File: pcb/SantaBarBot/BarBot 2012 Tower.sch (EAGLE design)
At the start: 52 parts, among them J2 POWER_JACKSLT, U1 ATMEGA328P, U2 SN75HVD179D, U3 742G04DBVR, U4 LMV324IDR, U5 L298, Y1 16MHz

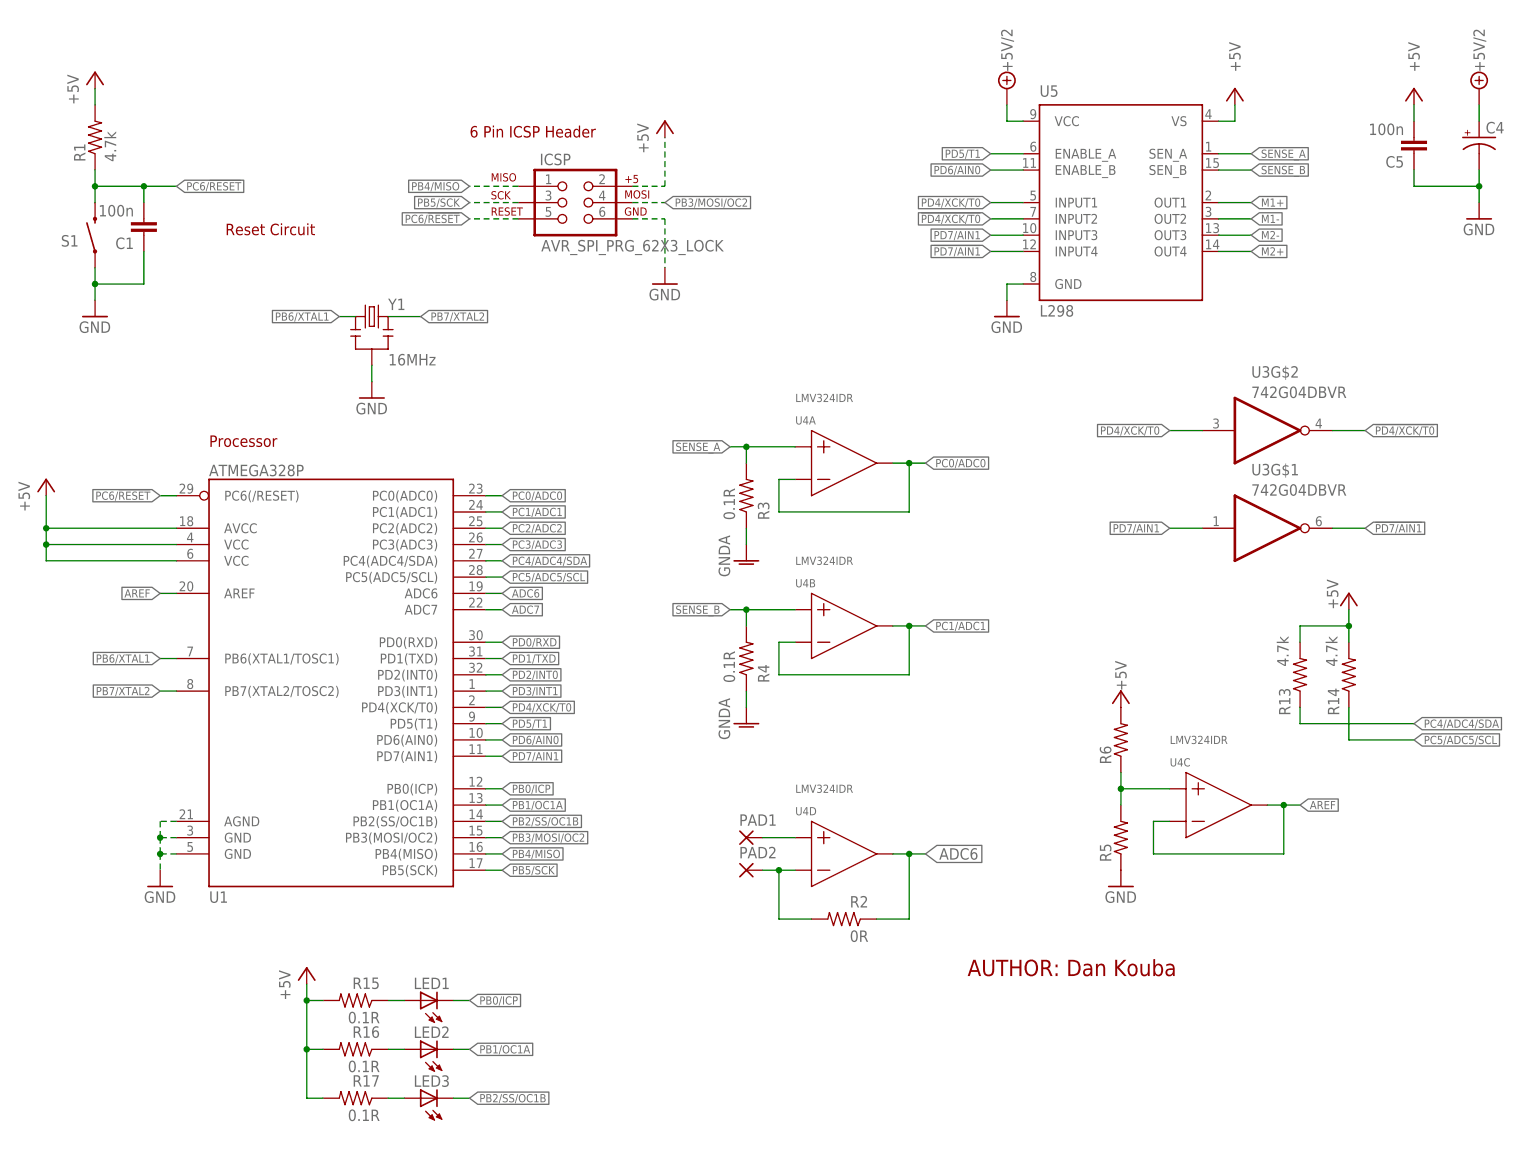
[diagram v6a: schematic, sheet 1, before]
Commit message: Finalizing PCB.  Added DC over ethernet capability, added micro-usb connector footprint, changed power jack to more standard one.  Added mounting holes.  Cleaned up some traces.  Added new renders (top and bottom)
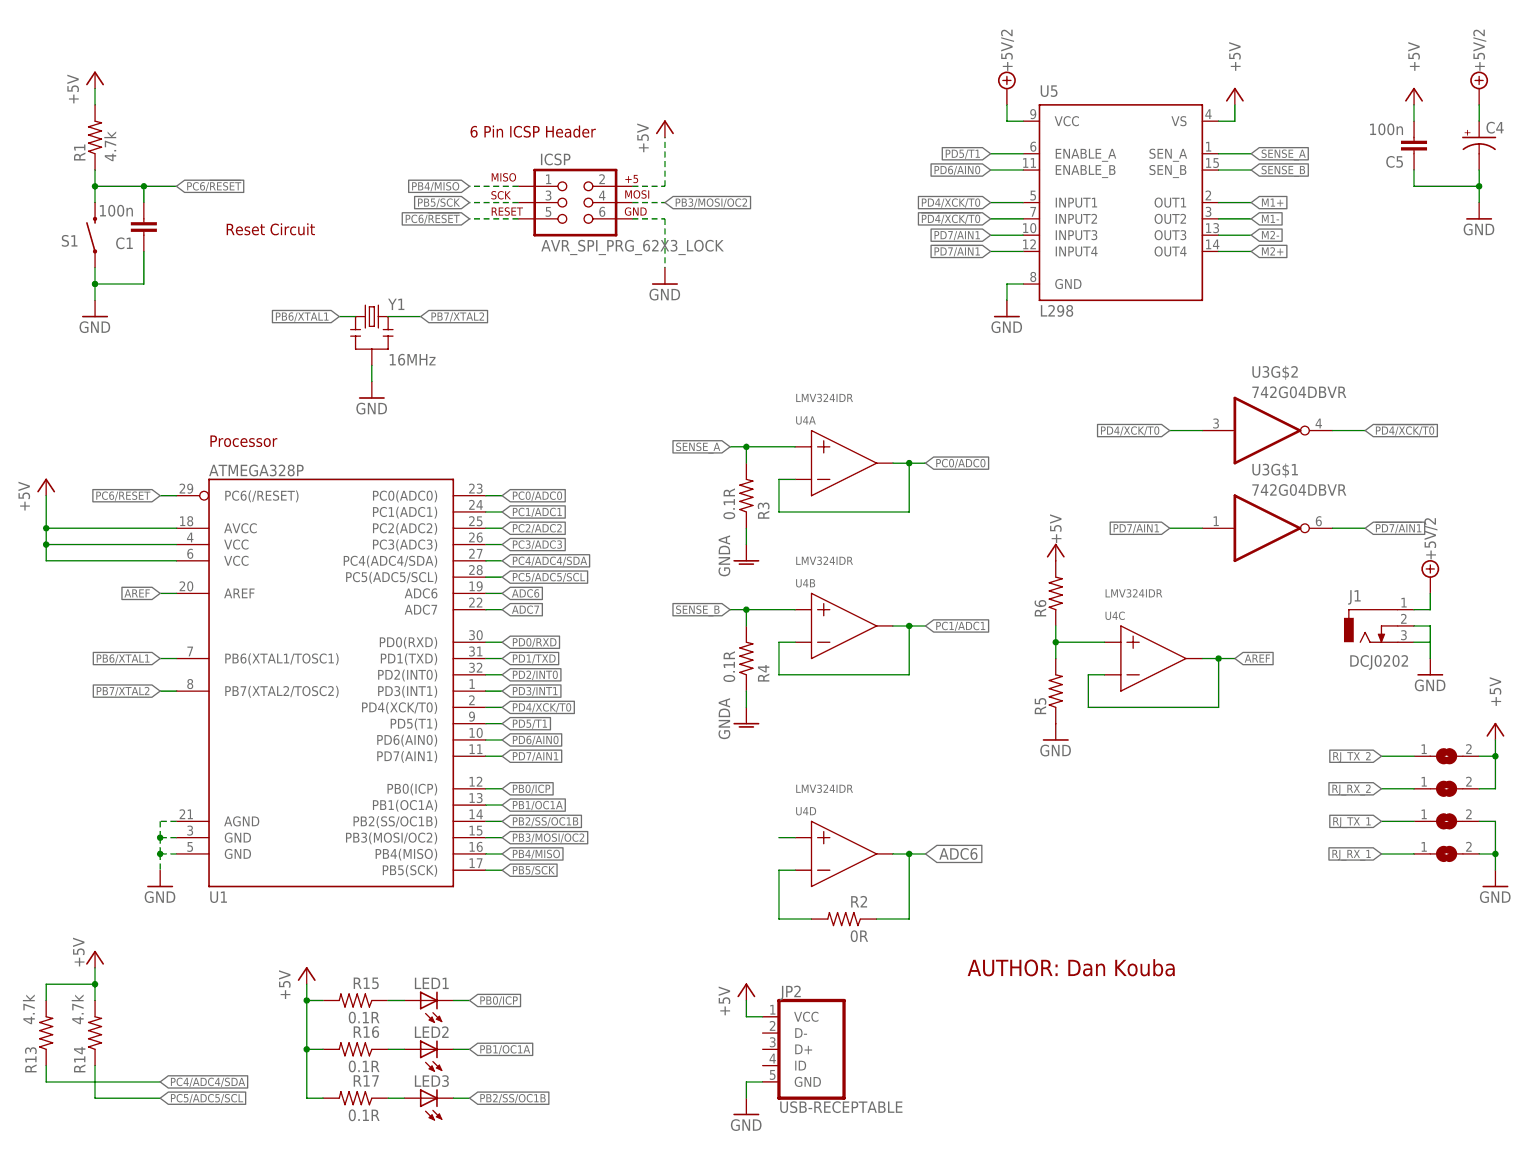
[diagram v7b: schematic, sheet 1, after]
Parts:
- removed J2: POWER_JACKSLT, SparkFun-Connectors:POWER_JACKSLT
- removed PAD1, PAD2: (no value), wirepad:1,6/0,8
- added J1: DCJ0202, con-jack:DCJ0202
- added JP2: USB-RECEPTABLE, daspilker:USB-RECEPTABLE
- added SJ1, SJ2, SJ3, SJ4: (no value), jumper:SJ
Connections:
- removed net N$3: PAD2.P, R2.2, U4D.-IN
- removed net RJ_RX_3: RX.3
- removed net RJ_RX_4: RX.4
- removed net RJ_RX_5: RX.5
- removed net RJ_RX_6: RX.6
- removed net RJ_RX_7: RX.7
- removed net RJ_RX_8: RX.8
- removed net RJ_TX_3: TX.3
- removed net RJ_TX_4: TX.4
- removed net RJ_TX_5: TX.5
- removed net RJ_TX_6: TX.6
- removed net RJ_TX_7: TX.7
- removed net RJ_TX_8: TX.8
- removed net TP1: PAD1.P, U4D.+IN
- new net RJ_RX_1: RX.3, RX.5, RX.7, SJ2.1
- new net RJ_RX_2: RX.4, RX.6, RX.8, SJ4.1
- new net RJ_TX_1: SJ1.1, TX.3, TX.5, TX.7
- new net RJ_TX_2: SJ3.1, TX.4, TX.6, TX.8
- new net U4D+: U4D.+IN
- new net U4D-: R2.2, U4D.-IN
- net +5V: now also JP2.VCC, SJ3.2, SJ4.2
- net +5V/2: now also J1.1; no longer J2.PWR
- net GND: now also J1.2, J1.3, JP2.GND, SJ1.2, SJ2.2; no longer J2.GND, J2.GNDBREAK
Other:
- moved on the sheet: R13, R14, R5, R6, U4C
